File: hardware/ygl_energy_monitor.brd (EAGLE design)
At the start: 50.8 x 52 mm, 5 parts

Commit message: fixed package
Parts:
- removed U$2: (no value), LEM:HO6SP33
- added SV1: (no value), con-lstb:MA03-1
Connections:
- net N$1: now also SV1.1; no longer U$2.V_CC
- net N$2: now also SV1.2; no longer U$2.GND
- net N$3: now also SV1.3; no longer U$2.V_OUT
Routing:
- net N$3: track 94.1 -> 61.5 mm
- net N$1: track 13.7 -> 10.2 mm
- net N$2: track 14.9 -> 15.5 mm
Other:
- board size 50.8 x 52 mm -> 49.6 x 52 mm
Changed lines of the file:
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@@
 <board>
 <plain>
-<wire x1="-0.0762" y1="8.6106" x2="50.6022" y2="8.4328" width="0" layer="20"/>
-<wire x1="50.6022" y1="8.4328" x2="50.526" y2="60.4522" width="0" layer="20"/>
-<wire x1="50.526" y1="60.4522" x2="-0.1524" y2="60.4522" width="0" layer="20"/>
+<wire x1="-0.0762" y1="8.6106" x2="49.4592" y2="8.4328" width="0" layer="20"/>
+<wire x1="49.4592" y1="8.4328" x2="49.383" y2="60.4522" width="0" layer="20"/>
+<wire x1="49.383" y1="60.4522" x2="-0.1524" y2="60.4522" width="0" layer="20"/>
 <wire x1="-0.1524" y1="60.4522" x2="-0.0762" y2="8.6106" width="0" layer="20"/>
-<hole x="1.778" y="58.4454" drill="3.175"/>
-<hole x="1.905" y="10.7188" drill="3.175"/>
-<hole x="48.5394" y="10.5918" drill="3.175"/>
-<hole x="48.5394" y="58.3946" drill="3.175"/>
+<hole x="2.1844" y="58.293" drill="3.175"/>
+<hole x="2.1844" y="10.8712" drill="3.175"/>
+<hole x="47.1424" y="10.7442" drill="3.175"/>
+<hole x="47.117" y="58.3946" drill="3.175"/>
 </plain>
 <attributes>
@@
 </autorouter>
 <elements>
-<element name="U$2" library="LEM" package="HO6SP33" value="" x="55.118" y="43.942" rot="R270"/>
 <element name="U$1" library="Spark" package="PHOTON" value="PHOTON_WITH_HEADERS" x="15.24" y="17.78"/>
 <element name="J2" library="SparkFun-Connectors" package="SCREWTERMINAL-3.5MM-2" value="" x="2.4638" y="43.8404" rot="R90">
@@
 <element name="R2" library="resistor" library_urn="urn:adsk.eagle:library:348" package="0207/10" package3d_urn="urn:adsk.eagle:package:25939/1" value="" x="10.4902" y="19.6596" rot="R90"/>
 <element name="R1" library="resistor" library_urn="urn:adsk.eagle:library:348" package="0207/10" package3d_urn="urn:adsk.eagle:package:25939/1" value="" x="10.3378" y="33.1724" rot="R270"/>
+<element name="SV1" library="con-lstb" library_urn="urn:adsk.eagle:library:162" package="MA03-1" package3d_urn="urn:adsk.eagle:package:8339/1" value="" x="44.2214" y="47.3964" rot="R270">
+<attribute name="MF" value="" x="44.2214" y="47.3964" size="1.778" layer="27" rot="R270" display="off"/>
+<attribute name="MPN" value="" x="44.2214" y="47.3964" size="1.778" layer="27" rot="R270" display="off"/>
+<attribute name="OC_FARNELL" value="unknown" x="44.2214" y="47.3964" size="1.778" layer="27" rot="R270" display="off"/>
+<attribute name="OC_NEWARK" value="unknown" x="44.2214" y="47.3964" size="1.778" layer="27" rot="R270" display="off"/>
+</element>
 </elements>
 <signals>
@@
 <signal name="N$1">
 <contactref element="U$1" pad="24"/>
-<contactref element="U$2" pad="V_CC"/>
-<wire x1="42.848" y1="44.926" x2="37.2364" y2="44.926" width="0.6096" layer="16"/>
-<wire x1="37.2364" y1="44.926" x2="37.2364" y2="49.8856" width="0.6096" layer="16"/>
-<wire x1="37.2364" y1="49.8856" x2="34.29" y2="49.8856" width="0.6096" layer="16"/>
 <wire x1="34.29" y1="49.8856" x2="34.29" y2="50.038" width="0.6096" layer="16"/>
+<contactref element="SV1" pad="1"/>
+<wire x1="34.29" y1="50.038" x2="44.2214" y2="50.038" width="0.508" layer="16"/>
+<wire x1="44.2214" y1="50.038" x2="44.2214" y2="49.9364" width="0.508" layer="16"/>
 </signal>
 <signal name="N$2">
 <contactref element="U$1" pad="21"/>
-<contactref element="U$2" pad="GND"/>
 <wire x1="34.4678" y1="42.5196" x2="34.544" y2="41.91" width="0.4064" layer="16"/>
-<wire x1="44.848" y1="46.18" x2="44.848" y2="42.418" width="0.6096" layer="16"/>
-<wire x1="44.848" y1="42.418" x2="34.29" y2="42.418" width="0.6096" layer="16"/>
+<contactref element="SV1" pad="2"/>
+<wire x1="34.29" y1="42.418" x2="39.2176" y2="42.418" width="0.508" layer="16"/>
+<wire x1="39.2176" y1="47.3964" x2="44.2214" y2="47.3964" width="0.508" layer="16"/>
+<wire x1="39.2176" y1="42.418" x2="39.2176" y2="47.3964" width="0.508" layer="16"/>
 <wire x1="34.29" y1="42.418" x2="34.4678" y2="42.5196" width="0" layer="19" extent="16-16"/>
 </signal>
 <signal name="N$3">
-<contactref element="U$2" pad="V_OUT"/>
 <contactref element="U$1" pad="12"/>
-<wire x1="47.5488" y1="15.0622" x2="47.5488" y2="53.6448" width="0.6096" layer="16"/>
-<wire x1="47.5488" y1="53.6448" x2="39.5986" y2="53.6448" width="0.6096" layer="16"/>
-<wire x1="39.5986" y1="53.6448" x2="39.5986" y2="47.434" width="0.6096" layer="16"/>
-<wire x1="39.5986" y1="47.434" x2="42.848" y2="47.434" width="0.6096" layer="16"/>
-<wire x1="16.51" y1="22.098" x2="16.51" y2="15.0622" width="0.6096" layer="16"/>
-<wire x1="16.51" y1="15.0622" x2="47.5488" y2="15.0622" width="0.6096" layer="16"/>
-</signal>
-<signal name="N$8">
-<via x="42.8244" y="49.9618" extent="1-16" drill="1.2" diameter="0.8128"/>
-</signal>
-<signal name="N$9">
-<via x="44.831" y="48.9458" extent="1-16" drill="1.2" diameter="0.8128"/>
-</signal>
-<signal name="N$10">
-<via x="42.8752" y="47.4218" extent="1-16" drill="1.2" diameter="0.8128"/>
-</signal>
-<signal name="N$11">
-<via x="44.8564" y="46.1772" extent="1-16" drill="1.2" diameter="0.8128"/>
-</signal>
-<signal name="N$12">
-<via x="42.8498" y="44.9326" extent="1-16" drill="1.2" diameter="0.8128"/>
+<contactref element="SV1" pad="3"/>
+<wire x1="44.2214" y1="44.8564" x2="44.2214" y2="16.5862" width="0.508" layer="16"/>
+<wire x1="44.2214" y1="16.5862" x2="16.5608" y2="16.5862" width="0.508" layer="16"/>
+<wire x1="16.5608" y1="16.5862" x2="16.5608" y2="22.098" width="0.508" layer="16"/>
+<wire x1="16.5608" y1="22.098" x2="16.51" y2="22.098" width="0.508" layer="16"/>
 </signal>
 <signal name="VIN">

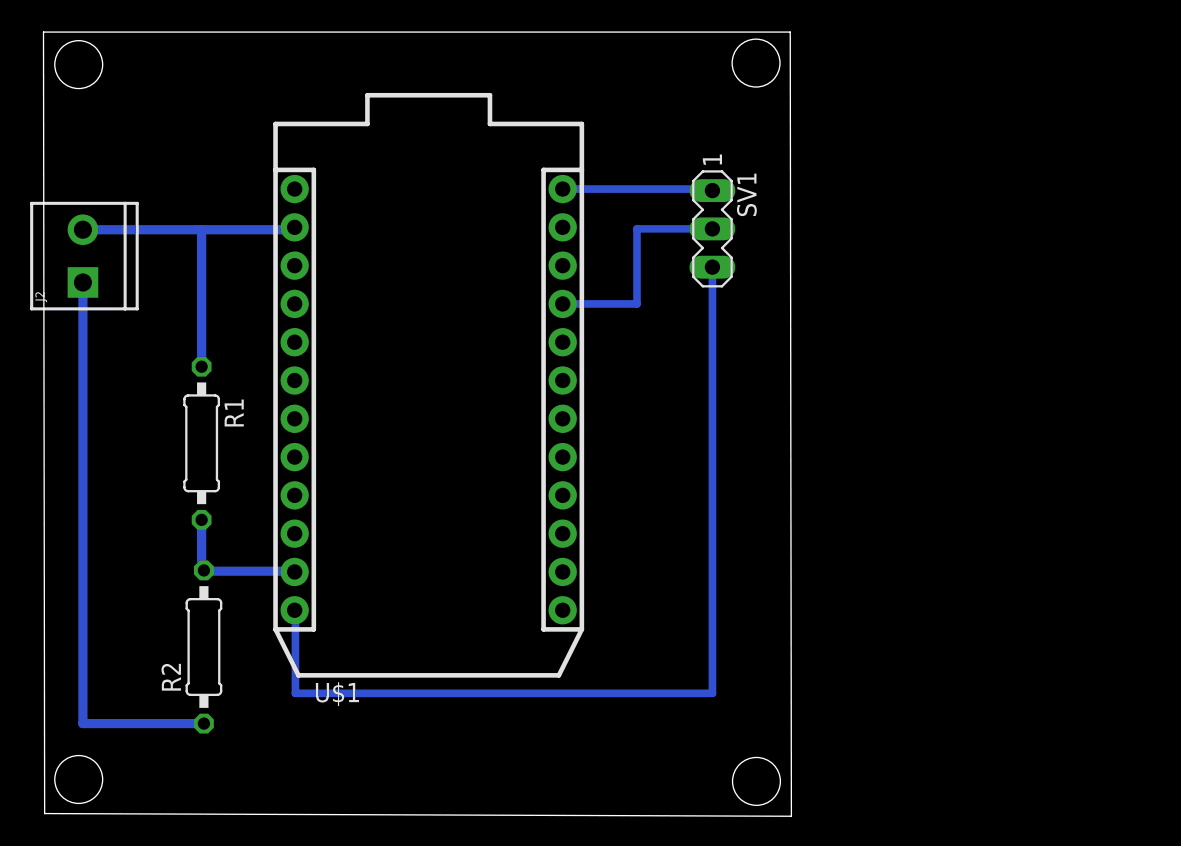
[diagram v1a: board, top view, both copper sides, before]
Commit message: avoid the braze?
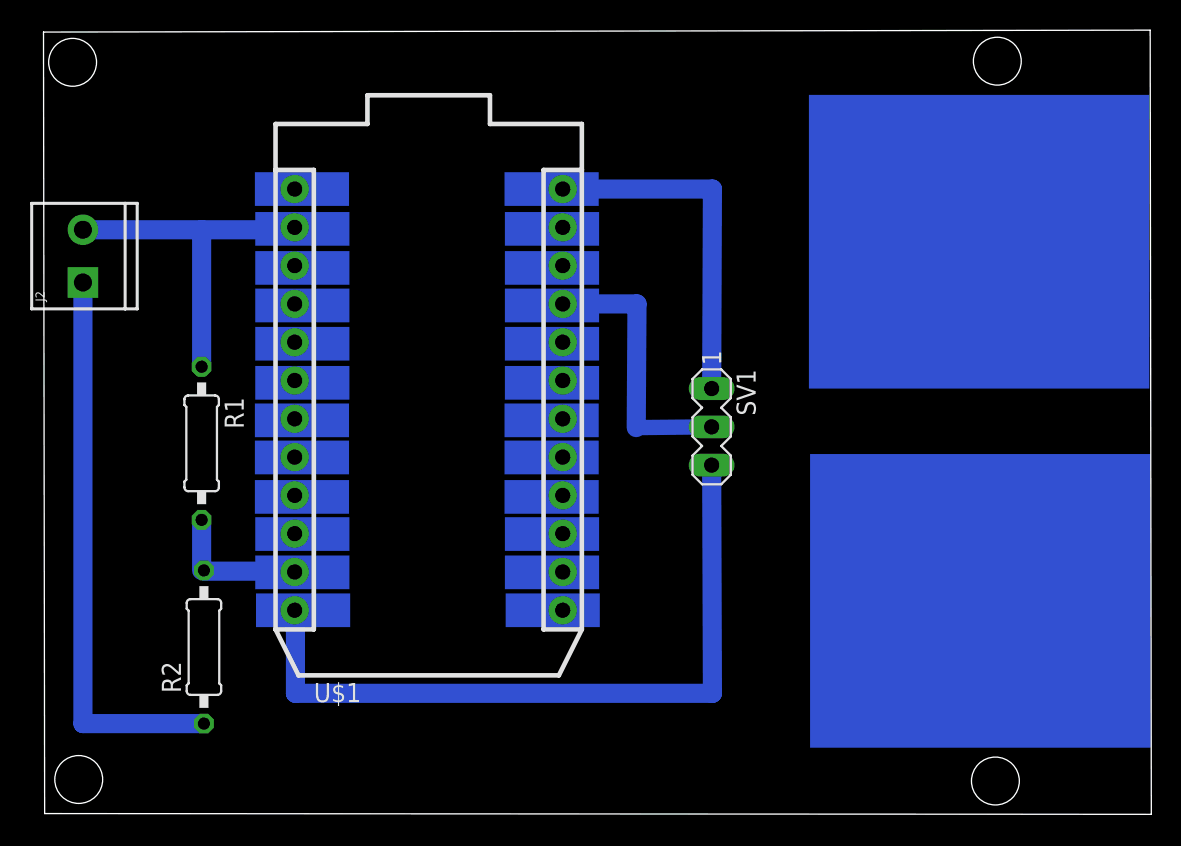
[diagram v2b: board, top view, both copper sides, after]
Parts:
- moved SV1 13.1 mm to (44.2, 34.3)
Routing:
- net N$1: track 10.2 -> 23.3 mm
- net N$3: track 61.5 -> 48.4 mm
- net N$2: track 15.5 -> 18.8 mm
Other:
- board size 49.6 x 52 mm -> 73.5 x 52 mm
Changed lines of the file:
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@@
 <setting verticaltext="up"/>
 </settings>
-<grid distance="0.001" unitdist="inch" unit="inch" style="lines" multiple="1" display="no" altdistance="0.025" altunitdist="inch" altunit="inch"/>
+<grid distance="0.001" unitdist="inch" unit="mm" style="lines" multiple="1" display="no" altdistance="0.025" altunitdist="inch" altunit="inch"/>
 <layers>
-<layer number="1" name="Top" color="4" fill="1" visible="no" active="yes"/>
+<layer number="1" name="Top" color="4" fill="1" visible="yes" active="yes"/>
 <layer number="2" name="Route2" color="1" fill="3" visible="no" active="no"/>
 <layer number="3" name="Route3" color="4" fill="3" visible="no" active="no"/>
@@
 <layer number="44" name="Drills" color="7" fill="1" visible="no" active="yes"/>
 <layer number="45" name="Holes" color="7" fill="1" visible="yes" active="yes"/>
-<layer number="46" name="Milling" color="3" fill="1" visible="no" active="yes"/>
+<layer number="46" name="Milling" color="3" fill="1" visible="yes" active="yes"/>
 <layer number="47" name="Measures" color="7" fill="1" visible="no" active="yes"/>
 <layer number="48" name="Document" color="7" fill="1" visible="yes" active="yes"/>
@@
 <board>
 <plain>
-<wire x1="-0.0762" y1="8.6106" x2="49.4592" y2="8.4328" width="0" layer="20"/>
-<wire x1="49.4592" y1="8.4328" x2="49.383" y2="60.4522" width="0" layer="20"/>
-<wire x1="49.383" y1="60.4522" x2="-0.1524" y2="60.4522" width="0" layer="20"/>
+<wire x1="-0.0762" y1="8.6106" x2="73.3352" y2="8.5598" width="0" layer="20"/>
+<wire x1="73.3352" y1="8.5598" x2="73.259" y2="60.5792" width="0" layer="20"/>
+<wire x1="73.259" y1="60.5792" x2="-0.1524" y2="60.4522" width="0" layer="20"/>
 <wire x1="-0.1524" y1="60.4522" x2="-0.0762" y2="8.6106" width="0" layer="20"/>
-<hole x="2.1844" y="58.293" drill="3.175"/>
+<hole x="1.778" y="58.4454" drill="3.175"/>
 <hole x="2.1844" y="10.8712" drill="3.175"/>
-<hole x="47.1424" y="10.7442" drill="3.175"/>
-<hole x="47.117" y="58.3946" drill="3.175"/>
+<hole x="62.992" y="10.7696" drill="3.175"/>
+<hole x="63.119" y="58.5216" drill="3.175"/>
+<rectangle x1="13.8684" y1="48.9204" x2="20.1168" y2="51.1556" layer="16"/>
+<rectangle x1="13.8938" y1="46.2788" x2="20.1422" y2="48.514" layer="16"/>
+<rectangle x1="13.8938" y1="43.688" x2="20.1422" y2="45.9232" layer="16"/>
+<rectangle x1="13.8938" y1="41.1988" x2="20.1422" y2="43.434" layer="16"/>
+<rectangle x1="13.8938" y1="38.6588" x2="20.1422" y2="40.894" layer="16"/>
+<rectangle x1="13.8938" y1="36.068" x2="20.1422" y2="38.3032" layer="16"/>
+<rectangle x1="13.8684" y1="33.5788" x2="20.1168" y2="35.814" layer="16"/>
+<rectangle x1="13.8684" y1="31.115" x2="20.1168" y2="33.3502" layer="16"/>
+<rectangle x1="13.8684" y1="28.4988" x2="20.1168" y2="30.734" layer="16"/>
+<rectangle x1="13.8938" y1="26.035" x2="20.1422" y2="28.2702" layer="16"/>
+<rectangle x1="13.8938" y1="23.495" x2="20.1422" y2="25.7302" layer="16"/>
+<rectangle x1="13.9446" y1="20.9804" x2="20.193" y2="23.2156" layer="16"/>
+<rectangle x1="30.4292" y1="48.9204" x2="36.6776" y2="51.1556" layer="16"/>
+<rectangle x1="30.4546" y1="46.2788" x2="36.703" y2="48.514" layer="16"/>
+<rectangle x1="30.4546" y1="43.688" x2="36.703" y2="45.9232" layer="16"/>
+<rectangle x1="30.4546" y1="41.1988" x2="36.703" y2="43.434" layer="16"/>
+<rectangle x1="30.4546" y1="38.6588" x2="36.703" y2="40.894" layer="16"/>
+<rectangle x1="30.4546" y1="36.068" x2="36.703" y2="38.3032" layer="16"/>
+<rectangle x1="30.4292" y1="33.5788" x2="36.6776" y2="35.814" layer="16"/>
+<rectangle x1="30.4292" y1="31.115" x2="36.6776" y2="33.3502" layer="16"/>
+<rectangle x1="30.4292" y1="28.4988" x2="36.6776" y2="30.734" layer="16"/>
+<rectangle x1="30.4546" y1="26.035" x2="36.703" y2="28.2702" layer="16"/>
+<rectangle x1="30.4546" y1="23.495" x2="36.703" y2="25.7302" layer="16"/>
+<rectangle x1="30.5054" y1="20.9804" x2="36.7538" y2="23.2156" layer="16"/>
+<rectangle x1="0.6096" y1="58.0898" x2="0.8382" y2="58.2168" layer="16"/>
+<rectangle x1="60.071" y1="38.608" x2="70.5612" y2="52.2224" layer="45"/>
+<rectangle x1="60.071" y1="16.5354" x2="70.5612" y2="30.1498" layer="45"/>
+<rectangle x1="50.6222" y1="36.8046" x2="73.2028" y2="56.2864" layer="16"/>
+<rectangle x1="50.6984" y1="12.9794" x2="73.279" y2="32.4612" layer="16"/>
 </plain>
 <attributes>
@@
 <element name="R2" library="resistor" library_urn="urn:adsk.eagle:library:348" package="0207/10" package3d_urn="urn:adsk.eagle:package:25939/1" value="" x="10.4902" y="19.6596" rot="R90"/>
 <element name="R1" library="resistor" library_urn="urn:adsk.eagle:library:348" package="0207/10" package3d_urn="urn:adsk.eagle:package:25939/1" value="" x="10.3378" y="33.1724" rot="R270"/>
-<element name="SV1" library="con-lstb" library_urn="urn:adsk.eagle:library:162" package="MA03-1" package3d_urn="urn:adsk.eagle:package:8339/1" value="" x="44.2214" y="47.3964" rot="R270">
-<attribute name="MF" value="" x="44.2214" y="47.3964" size="1.778" layer="27" rot="R270" display="off"/>
-<attribute name="MPN" value="" x="44.2214" y="47.3964" size="1.778" layer="27" rot="R270" display="off"/>
-<attribute name="OC_FARNELL" value="unknown" x="44.2214" y="47.3964" size="1.778" layer="27" rot="R270" display="off"/>
-<attribute name="OC_NEWARK" value="unknown" x="44.2214" y="47.3964" size="1.778" layer="27" rot="R270" display="off"/>
+<element name="SV1" library="con-lstb" library_urn="urn:adsk.eagle:library:162" package="MA03-1" package3d_urn="urn:adsk.eagle:package:8339/1" value="" x="44.1706" y="34.2646" rot="R270">
+<attribute name="MF" value="" x="44.1706" y="34.2646" size="1.778" layer="27" rot="R270" display="off"/>
+<attribute name="MPN" value="" x="44.1706" y="34.2646" size="1.778" layer="27" rot="R270" display="off"/>
+<attribute name="OC_FARNELL" value="unknown" x="44.1706" y="34.2646" size="1.778" layer="27" rot="R270" display="off"/>
+<attribute name="OC_NEWARK" value="unknown" x="44.1706" y="34.2646" size="1.778" layer="27" rot="R270" display="off"/>
 </element>
 </elements>
@@
 <wire x1="34.29" y1="49.8856" x2="34.29" y2="50.038" width="0.6096" layer="16"/>
 <contactref element="SV1" pad="1"/>
-<wire x1="34.29" y1="50.038" x2="44.2214" y2="50.038" width="0.508" layer="16"/>
-<wire x1="44.2214" y1="50.038" x2="44.2214" y2="49.9364" width="0.508" layer="16"/>
+<wire x1="34.29" y1="50.038" x2="44.2214" y2="50.038" width="1.27" layer="16"/>
+<wire x1="44.2214" y1="50.038" x2="44.1706" y2="36.8046" width="1.27" layer="16"/>
 </signal>
 <signal name="N$2">
@@
 <wire x1="34.4678" y1="42.5196" x2="34.544" y2="41.91" width="0.4064" layer="16"/>
 <contactref element="SV1" pad="2"/>
-<wire x1="34.29" y1="42.418" x2="39.2176" y2="42.418" width="0.508" layer="16"/>
-<wire x1="39.2176" y1="47.3964" x2="44.2214" y2="47.3964" width="0.508" layer="16"/>
-<wire x1="39.2176" y1="42.418" x2="39.2176" y2="47.3964" width="0.508" layer="16"/>
+<wire x1="34.29" y1="42.418" x2="39.2176" y2="42.418" width="1.27" layer="16"/>
+<wire x1="39.1668" y1="34.2138" x2="44.1706" y2="34.2646" width="1.016" layer="16"/>
+<wire x1="39.2176" y1="42.418" x2="39.1668" y2="34.2138" width="1.27" layer="16"/>
 <wire x1="34.29" y1="42.418" x2="34.4678" y2="42.5196" width="0" layer="19" extent="16-16"/>
 </signal>
@@
 <contactref element="U$1" pad="12"/>
 <contactref element="SV1" pad="3"/>
-<wire x1="44.2214" y1="44.8564" x2="44.2214" y2="16.5862" width="0.508" layer="16"/>
-<wire x1="44.2214" y1="16.5862" x2="16.5608" y2="16.5862" width="0.508" layer="16"/>
-<wire x1="16.5608" y1="16.5862" x2="16.5608" y2="22.098" width="0.508" layer="16"/>
+<wire x1="44.1706" y1="31.7246" x2="44.2214" y2="16.5862" width="1.27" layer="16"/>
+<wire x1="44.2214" y1="16.5862" x2="16.5608" y2="16.5862" width="1.27" layer="16"/>
+<wire x1="16.5608" y1="16.5862" x2="16.5608" y2="22.098" width="1.27" layer="16"/>
 <wire x1="16.5608" y1="22.098" x2="16.51" y2="22.098" width="0.508" layer="16"/>
 </signal>
@@
 <contactref element="R1" pad="2"/>
 <wire x1="16.51" y1="24.6888" x2="16.51" y2="24.638" width="0.4064" layer="16"/>
-<wire x1="10.3378" y1="28.0924" x2="10.3378" y2="24.7396" width="0.6096" layer="16"/>
+<wire x1="10.3378" y1="28.0924" x2="10.3378" y2="24.7396" width="1.27" layer="16"/>
 <wire x1="10.3378" y1="24.7396" x2="10.4902" y2="24.7396" width="0.6096" layer="16"/>
 <wire x1="10.4902" y1="24.7396" x2="10.4902" y2="24.6888" width="0.6096" layer="16"/>
-<wire x1="10.4902" y1="24.6888" x2="16.51" y2="24.6888" width="0.6096" layer="16"/>
+<wire x1="10.4902" y1="24.6888" x2="16.51" y2="24.6888" width="1.27" layer="16"/>
 </signal>
 <signal name="N$4">
@@
 <contactref element="R1" pad="1"/>
 <contactref element="J2" pad="2"/>
-<wire x1="2.4638" y1="47.3404" x2="10.3378" y2="47.3404" width="0.6096" layer="16"/>
-<wire x1="10.3378" y1="47.3404" x2="16.51" y2="47.3404" width="0.6096" layer="16"/>
+<wire x1="2.4638" y1="47.3404" x2="10.3378" y2="47.3404" width="1.27" layer="16"/>
+<wire x1="10.3378" y1="47.3404" x2="16.51" y2="47.3404" width="1.27" layer="16"/>
 <wire x1="16.51" y1="47.3404" x2="16.51" y2="47.498" width="0.6096" layer="16"/>
-<wire x1="10.3378" y1="47.3404" x2="10.3378" y2="38.2524" width="0.6096" layer="16"/>
+<wire x1="10.3378" y1="47.3404" x2="10.3378" y2="38.2524" width="1.27" layer="16"/>
 </signal>
 <signal name="N$5">
 <contactref element="J2" pad="1"/>
 <contactref element="R2" pad="1"/>
-<wire x1="2.4638" y1="43.8404" x2="2.4638" y2="14.5796" width="0.6096" layer="16"/>
-<wire x1="2.4638" y1="14.5796" x2="10.4902" y2="14.5796" width="0.6096" layer="16"/>
+<wire x1="2.4638" y1="43.8404" x2="2.4638" y2="14.5796" width="1.27" layer="16"/>
+<wire x1="2.4638" y1="14.5796" x2="10.4902" y2="14.5796" width="1.27" layer="16"/>
 </signal>
 </signals>
